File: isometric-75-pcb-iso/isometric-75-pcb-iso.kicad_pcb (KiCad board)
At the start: 2 copper layers, 308.8 x 123.5 mm, 314 parts, among them J101 USB, J102 SPI, J103 Conn_01x06_Male, Q101 AO3400A, SW101 RST, SW102 BOOT, SW201 Rotary_Encoder_Switch, U101 XC6206P332MR, U102 STM32F072CBTx, U301 74LVC1G125

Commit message: changed divider resistors to save power
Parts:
- R104, R105: value 10k -> 50k

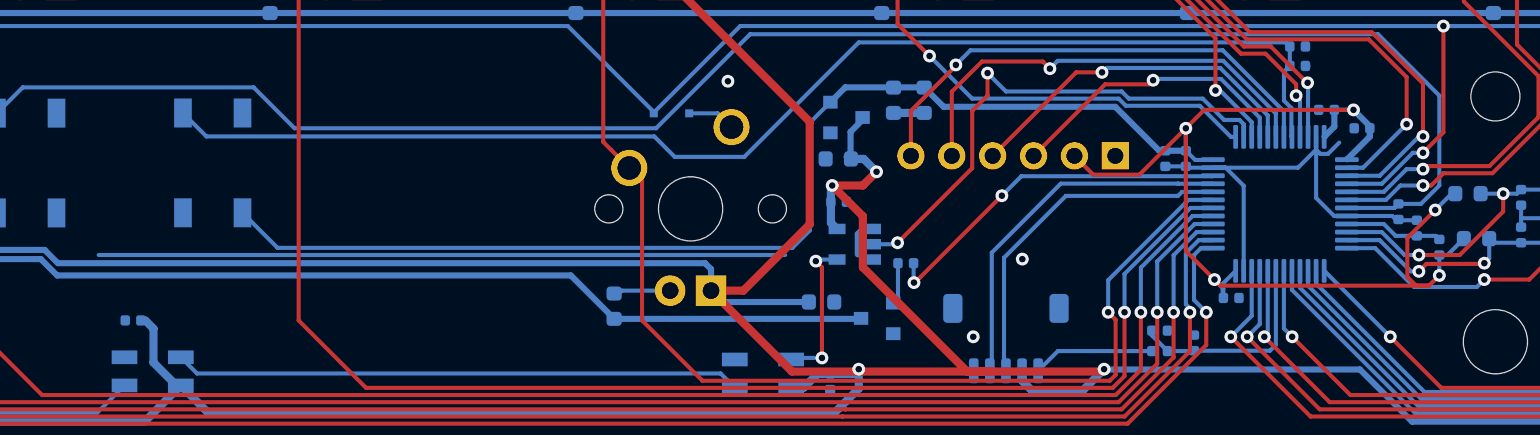
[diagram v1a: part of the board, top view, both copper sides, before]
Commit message: minor layout improvements
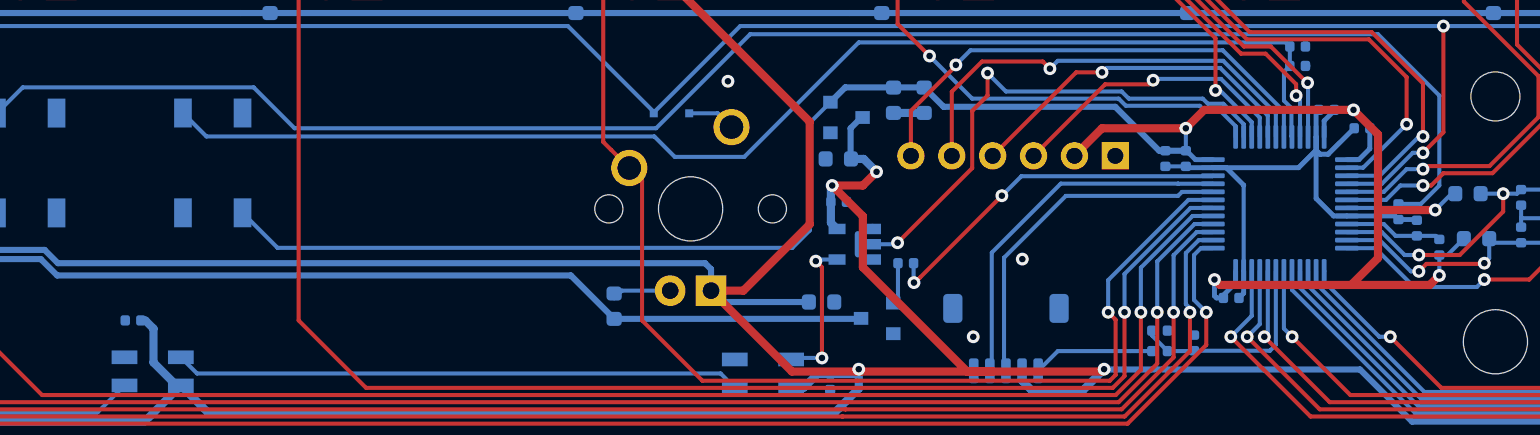
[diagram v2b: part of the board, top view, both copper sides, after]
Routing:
- net GND: track 874.4 -> 846.4 mm
- net +3V3: track 138.4 -> 137.5 mm
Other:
- net class Power: trace_width 0.508 -> 0.3048

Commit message: minor layout fixes (thanks gLu3xb3rchi)
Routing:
- net LED_PWM: track 22.5 -> 20.8 mm, vias 2 -> 0
- net GND: vias 12 -> 23
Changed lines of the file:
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@@
     (thickness 1.6)
     (drawings 13)
-    (tracks 2289)
+    (tracks 2293)
     (zones 0)
     (modules 314)
@@
   (gr_arc (start -7.125 -7.125) (end -7.125 -9.5) (angle -90) (layer Edge.Cuts) (width 0.05))
   (via (at 141.732 102.87) (size 0.8) (drill 0.4) (layers F.Cu B.Cu) (net 1))
-  (segment (start 155.484 103.6035) (end 155.484 98.310904) (width 0.254) (layer B.Cu) (net 1))
   (segment (start 161.103904 100.191) (end 159.984 99.071096) (width 0.254) (layer B.Cu) (net 1))
   (segment (start 161.8965 100.191) (end 161.103904 100.191) (width 0.254) (layer B.Cu) (net 1))
   (segment (start 159.984 96.016) (end 159.984 95.2785) (width 0.254) (layer B.Cu) (net 1))
-  (segment (start 159.984 99.071096) (end 159.984 96.016) (width 0.254) (layer B.Cu) (net 1))
   (segment (start 161.424096 95.631) (end 160.721586 96.33351) (width 0.254) (layer B.Cu) (net 1))
-  (segment (start 160.721586 96.33351) (end 160.246414 96.33351) (width 0.254) (layer B.Cu) (net 1))
-  (segment (start 160.246414 96.33351) (end 159.984 96.071096) (width 0.254) (layer B.Cu) (net 1))
   (segment (start 159.984 96.071096) (end 159.984 96.016) (width 0.254) (layer B.Cu) (net 1))
-  (segment (start 159.984 96.071096) (end 158.864096 97.191) (width 0.254) (layer B.Cu) (net 1))
   (segment (start 151.892 97.028) (end 152.055 97.191) (width 0.254) (layer B.Cu) (net 1))
   (segment (start 162.352 94.742) (end 162.313096 94.742) (width 0.381) (layer B.Cu) (net 1))
@@
   (segment (start 162.349014 94.742) (end 160.732104 96.35891) (width 0.3048) (layer B.Cu) (net 1))
   (segment (start 162.352 94.742) (end 162.349014 94.742) (width 0.3048) (layer B.Cu) (net 1))
-  (segment (start 158.900014 97.191) (end 153.5715 97.191) (width 0.3048) (layer B.Cu) (net 1))
-  (segment (start 159.984 96.107014) (end 158.900014 97.191) (width 0.3048) (layer B.Cu) (net 1))
   (segment (start 159.984 95.2785) (end 159.984 96.107014) (width 0.3048) (layer B.Cu) (net 1))
-  (segment (start 159.984 99.107014) (end 159.984 95.2785) (width 0.3048) (layer B.Cu) (net 1))
   (segment (start 161.067986 100.191) (end 159.984 99.107014) (width 0.3048) (layer B.Cu) (net 1))
   (segment (start 161.8965 100.191) (end 161.067986 100.191) (width 0.3048) (layer B.Cu) (net 1))
@@
   (segment (start 155.484 103.6035) (end 155.484 104.993) (width 0.3048) (layer B.Cu) (net 1))
   (segment (start 154.400014 97.191) (end 153.5715 97.191) (width 0.3048) (layer B.Cu) (net 1))
-  (segment (start 155.484 98.274986) (end 154.400014 97.191) (width 0.3048) (layer B.Cu) (net 1))
   (segment (start 155.484 98.310904) (end 155.484 98.274986) (width 0.3048) (layer B.Cu) (net 1))
   (segment (start 159.984 93.762) (end 159.984 95.2785) (width 0.3048) (layer B.Cu) (net 1))
   (segment (start 160.147 93.599) (end 159.984 93.762) (width 0.3048) (layer B.Cu) (net 1))
+  (via (at 132.842 99.314) (size 0.8) (drill 0.4) (layers F.Cu B.Cu) (net 1))
+  (via (at 132.842 95.504) (size 0.8) (drill 0.4) (layers F.Cu B.Cu) (net 1))
+  (via (at 126.746 95.504) (size 0.8) (drill 0.4) (layers F.Cu B.Cu) (net 1))
+  (via (at 108.458 107.696) (size 0.8) (drill 0.4) (layers F.Cu B.Cu) (net 1))
+  (via (at 82.296 107.696) (size 0.8) (drill 0.4) (layers F.Cu B.Cu) (net 1))
+  (via (at 64.77 107.696) (size 0.8) (drill 0.4) (layers F.Cu B.Cu) (net 1))
+  (via (at 53.594 107.696) (size 0.8) (drill 0.4) (layers F.Cu B.Cu) (net 1))
+  (via (at 35.56 107.696) (size 0.8) (drill 0.4) (layers F.Cu B.Cu) (net 1))
+  (via (at 18.796 107.696) (size 0.8) (drill 0.4) (layers F.Cu B.Cu) (net 1))
+  (via (at -4.826 107.696) (size 0.8) (drill 0.4) (layers F.Cu B.Cu) (net 1))
+  (segment (start 160.246414 96.33351) (end 159.984 96.071096) (width 0.254) (layer B.Cu) (net 1))
+  (segment (start 159.984 96.107014) (end 158.900014 97.191) (width 0.3048) (layer B.Cu) (net 1))
+  (segment (start 160.721586 96.33351) (end 160.246414 96.33351) (width 0.254) (layer B.Cu) (net 1))
+  (segment (start 159.984 96.071096) (end 158.864096 97.191) (width 0.254) (layer B.Cu) (net 1))
+  (segment (start 155.484 98.274986) (end 154.400014 97.191) (width 0.3048) (layer B.Cu) (net 1))
+  (segment (start 158.900014 97.191) (end 153.5715 97.191) (width 0.3048) (layer B.Cu) (net 1))
+  (segment (start 159.984 99.107014) (end 159.984 95.2785) (width 0.3048) (layer B.Cu) (net 1))
+  (segment (start 159.984 99.071096) (end 159.984 96.016) (width 0.254) (layer B.Cu) (net 1))
+  (segment (start 155.484 103.6035) (end 155.484 98.310904) (width 0.254) (layer B.Cu) (net 1))
+  (via (at 157.734 99.441) (size 0.8) (drill 0.4) (layers F.Cu B.Cu) (net 1))
   (segment (start 150.622 96.139) (end 151.892 96.139) (width 0.381) (layer B.Cu) (net 2))
   (segment (start 151.892 96.058) (end 151.892 94.742) (width 0.254) (layer B.Cu) (net 2))
@@
   (segment (start 167.64 98.298) (end 167.64 92.71) (width 0.254) (layer B.Cu) (net 198))
   (segment (start 163.83 88.9) (end 124.821502 88.9) (width 0.254) (layer B.Cu) (net 198))
-  (segment (start 141.67348 97.72151) (end 140.462 98.93299) (width 0.254) (layer B.Cu) (net 199))
-  (segment (start 153.54099 97.72151) (end 141.67348 97.72151) (width 0.254) (layer B.Cu) (net 199))
+  (segment (start 142.81649 97.72151) (end 137.414 103.124) (width 0.254) (layer B.Cu) (net 199))
   (segment (start 153.5715 97.691) (end 153.54099 97.72151) (width 0.254) (layer B.Cu) (net 199))
-  (via (at 140.462 98.93299) (size 0.8) (drill 0.4) (layers F.Cu B.Cu) (net 199))
-  (segment (start 135.0645 104.3305) (end 135.001 104.3305) (width 0.254) (layer F.Cu) (net 199))
-  (segment (start 135.382 104.013) (end 135.0645 104.3305) (width 0.254) (layer F.Cu) (net 199))
-  (segment (start 140.462 98.933) (end 135.382 104.013) (width 0.254) (layer F.Cu) (net 199))
-  (segment (start 140.462 98.93299) (end 140.462 98.933) (width 0.254) (layer F.Cu) (net 199))
-  (via (at 135.001 104.3305) (size 0.8) (drill 0.4) (layers F.Cu B.Cu) (net 199))
-  (segment (start 134.978 104.3075) (end 135.001 104.3305) (width 0.254) (layer B.Cu) (net 199))
-  (segment (start 134.978 103.124) (end 134.978 104.3075) (width 0.254) (layer B.Cu) (net 199))
+  (segment (start 153.54099 97.72151) (end 142.81649 97.72151) (width 0.254) (layer B.Cu) (net 199))
+  (segment (start 134.978 103.124) (end 137.414 103.124) (width 0.254) (layer B.Cu) (net 199))
   (segment (start 178.863204 111.124956) (end 179.729 110.25916) (width 0.254) (layer B.Cu) (net 200))
   (segment (start 179.729 110.25916) (end 179.729 109.823) (width 0.254) (layer B.Cu) (net 200))

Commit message: renamed +5V net (thanks gLu3xb3rchi)
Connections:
- net LED+ renamed +5V

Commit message: changed switch footprint to accomodate millmax 7305
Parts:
- moved SW201 7.91 mm to (287.2, 7.50)
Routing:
- net ROW3: track 363.4 -> 362.7 mm
